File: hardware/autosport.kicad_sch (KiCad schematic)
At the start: 12 parts, among them J2 AS022-55SN

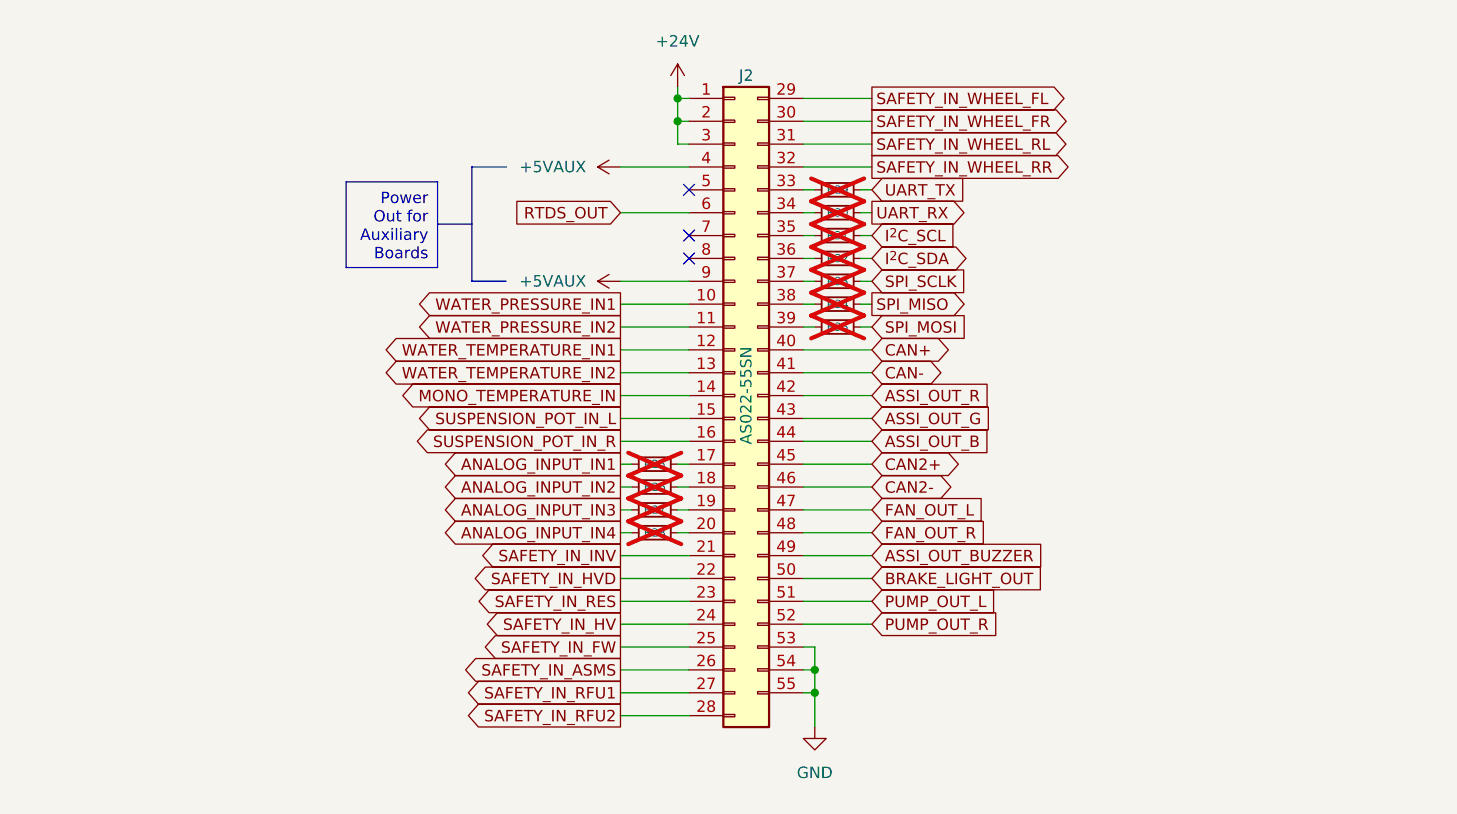
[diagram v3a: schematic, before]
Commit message: Improve the schematic according to the feedback
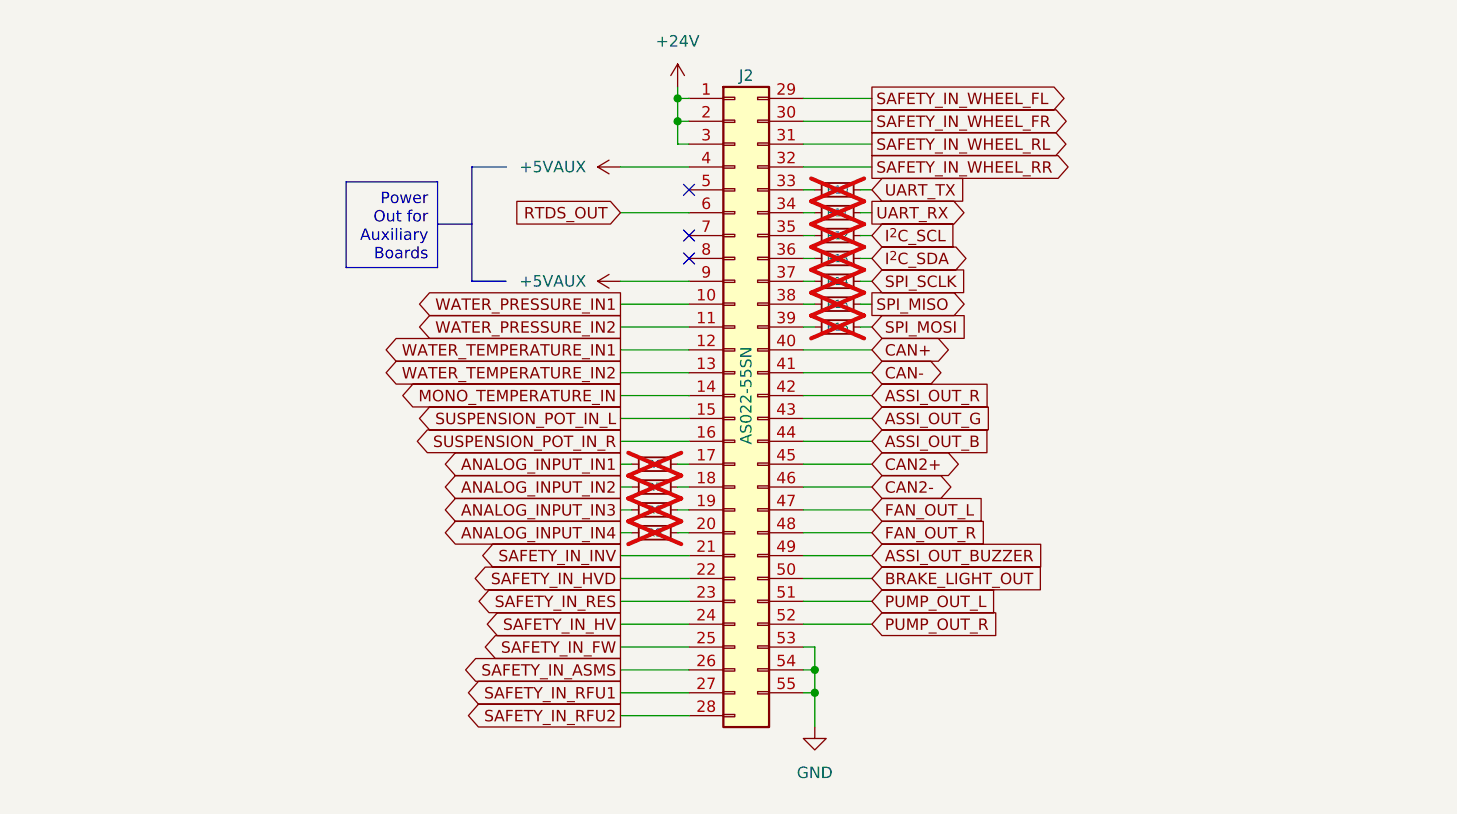
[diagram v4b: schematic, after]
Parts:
- renumbered R29 to R10, R30 to R11, R31 to R12, R32 to R13, R33 to R14, R34 to R15, R35 to R16, R25 to R6, R26 to R7, R27 to R8, R28 to R9
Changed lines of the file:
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@@
   (symbol (lib_id "Device:R_Small") (at 160.02 80.01 90) (unit 1)
     (in_bom yes) (on_board yes) (dnp yes)
-    (property "Reference" "R30" (at 160.02 80.01 90)
+    (property "Reference" "R11" (at 160.02 80.01 90)
       (effects (font (size 0.9 0.9)))
     )
@@
       (project "rearbox"
         (path "/b652b05a-4e3d-4ad1-b032-18886abe7d45/cf65c657-8245-46fb-8929-d241bd579513"
-          (reference "R30") (unit 1)
+          (reference "R11") (unit 1)
         )
       )
@@
   (symbol (lib_id "Device:R_Small") (at 160.02 87.63 90) (unit 1)
     (in_bom yes) (on_board yes) (dnp yes)
-    (property "Reference" "R33" (at 160.02 87.63 90)
+    (property "Reference" "R14" (at 160.02 87.63 90)
       (effects (font (size 0.9 0.9)))
     )
@@
       (project "rearbox"
         (path "/b652b05a-4e3d-4ad1-b032-18886abe7d45/cf65c657-8245-46fb-8929-d241bd579513"
-          (reference "R33") (unit 1)
+          (reference "R14") (unit 1)
         )
       )
@@
   (symbol (lib_id "Power_Ports:+5VAUX") (at 135.89 74.93 90) (unit 1)
     (in_bom yes) (on_board yes) (dnp no) (fields_autoplaced)
-    (property "Reference" "#PWR056" (at 139.7 74.93 0)
+    (property "Reference" "#PWR045" (at 139.7 74.93 0)
       (effects (font (size 1.27 1.27)) hide)
     )
@@
       (project "rearbox"
         (path "/b652b05a-4e3d-4ad1-b032-18886abe7d45/cf65c657-8245-46fb-8929-d241bd579513"
-          (reference "#PWR056") (unit 1)
+          (reference "#PWR045") (unit 1)
         )
       )
@@
   (symbol (lib_id "Device:R_Small") (at 160.02 82.55 90) (unit 1)
     (in_bom yes) (on_board yes) (dnp yes)
-    (property "Reference" "R31" (at 160.02 82.55 90)
+    (property "Reference" "R12" (at 160.02 82.55 90)
       (effects (font (size 0.9 0.9)))
     )
@@
       (project "rearbox"
         (path "/b652b05a-4e3d-4ad1-b032-18886abe7d45/cf65c657-8245-46fb-8929-d241bd579513"
-          (reference "R31") (unit 1)
+          (reference "R12") (unit 1)
         )
       )
@@
   (symbol (lib_id "power:+24V") (at 142.24 66.04 0) (unit 1)
     (in_bom yes) (on_board yes) (dnp no)
-    (property "Reference" "#PWR058" (at 142.24 69.85 0)
+    (property "Reference" "#PWR047" (at 142.24 69.85 0)
       (effects (font (size 1.27 1.27)) hide)
     )
@@
       (project "rearbox"
         (path "/b652b05a-4e3d-4ad1-b032-18886abe7d45/cf65c657-8245-46fb-8929-d241bd579513"
-          (reference "#PWR058") (unit 1)
+          (reference "#PWR047") (unit 1)
         )
       )
@@
   (symbol (lib_id "Device:R_Small") (at 160.02 77.47 90) (unit 1)
     (in_bom yes) (on_board yes) (dnp yes)
-    (property "Reference" "R29" (at 160.02 77.47 90)
+    (property "Reference" "R10" (at 160.02 77.47 90)
       (effects (font (size 0.9 0.9)))
     )
@@
       (project "rearbox"
         (path "/b652b05a-4e3d-4ad1-b032-18886abe7d45/cf65c657-8245-46fb-8929-d241bd579513"
-          (reference "R29") (unit 1)
+          (reference "R10") (unit 1)
         )
       )
@@
   (symbol (lib_id "Device:R_Small") (at 139.7 115.57 90) (unit 1)
     (in_bom yes) (on_board yes) (dnp yes)
-    (property "Reference" "R28" (at 139.7 115.57 90)
+    (property "Reference" "R9" (at 139.7 115.57 90)
       (effects (font (size 0.9 0.9)))
     )
@@
       (project "rearbox"
         (path "/b652b05a-4e3d-4ad1-b032-18886abe7d45/cf65c657-8245-46fb-8929-d241bd579513"
-          (reference "R28") (unit 1)
+          (reference "R9") (unit 1)
         )
       )
@@
   (symbol (lib_id "Power_Ports:+5VAUX") (at 135.89 87.63 90) (unit 1)
     (in_bom yes) (on_board yes) (dnp no) (fields_autoplaced)
-    (property "Reference" "#PWR057" (at 139.7 87.63 0)
+    (property "Reference" "#PWR046" (at 139.7 87.63 0)
       (effects (font (size 1.27 1.27)) hide)
     )
@@
       (project "rearbox"
         (path "/b652b05a-4e3d-4ad1-b032-18886abe7d45/cf65c657-8245-46fb-8929-d241bd579513"
-          (reference "#PWR057") (unit 1)
+          (reference "#PWR046") (unit 1)
         )
       )
@@
   (symbol (lib_id "Device:R_Small") (at 160.02 85.09 90) (unit 1)
     (in_bom yes) (on_board yes) (dnp yes)
-    (property "Reference" "R32" (at 160.02 85.09 90)
+    (property "Reference" "R13" (at 160.02 85.09 90)
       (effects (font (size 0.9 0.9)))
     )
@@
       (project "rearbox"
         (path "/b652b05a-4e3d-4ad1-b032-18886abe7d45/cf65c657-8245-46fb-8929-d241bd579513"
-          (reference "R32") (unit 1)
+          (reference "R13") (unit 1)
         )
       )
@@
   (symbol (lib_id "Device:R_Small") (at 139.7 110.49 90) (unit 1)
     (in_bom yes) (on_board yes) (dnp yes)
-    (property "Reference" "R26" (at 139.7 110.49 90)
+    (property "Reference" "R7" (at 139.7 110.49 90)
       (effects (font (size 0.9 0.9)))
     )
@@
       (project "rearbox"
         (path "/b652b05a-4e3d-4ad1-b032-18886abe7d45/cf65c657-8245-46fb-8929-d241bd579513"
-          (reference "R26") (unit 1)
+          (reference "R7") (unit 1)
         )
       )
@@
   (symbol (lib_id "power:GND") (at 157.48 137.16 0) (unit 1)
     (in_bom yes) (on_board yes) (dnp no) (fields_autoplaced)
-    (property "Reference" "#PWR059" (at 157.48 143.51 0)
+    (property "Reference" "#PWR048" (at 157.48 143.51 0)
       (effects (font (size 1.27 1.27)) hide)
     )
@@
       (project "rearbox"
         (path "/b652b05a-4e3d-4ad1-b032-18886abe7d45/cf65c657-8245-46fb-8929-d241bd579513"
-          (reference "#PWR059") (unit 1)
+          (reference "#PWR048") (unit 1)
         )
       )
@@
   (symbol (lib_id "Device:R_Small") (at 139.7 107.95 90) (unit 1)
     (in_bom yes) (on_board yes) (dnp yes)
-    (property "Reference" "R25" (at 139.7 107.95 90)
+    (property "Reference" "R6" (at 139.7 107.95 90)
       (effects (font (size 0.9 0.9)))
     )
@@
       (project "rearbox"
         (path "/b652b05a-4e3d-4ad1-b032-18886abe7d45/cf65c657-8245-46fb-8929-d241bd579513"
-          (reference "R25") (unit 1)
+          (reference "R6") (unit 1)
         )
       )
@@
   (symbol (lib_id "Device:R_Small") (at 160.02 90.17 90) (unit 1)
     (in_bom yes) (on_board yes) (dnp yes)
-    (property "Reference" "R34" (at 160.02 90.17 90)
+    (property "Reference" "R15" (at 160.02 90.17 90)
       (effects (font (size 0.9 0.9)))
     )
@@
       (project "rearbox"
         (path "/b652b05a-4e3d-4ad1-b032-18886abe7d45/cf65c657-8245-46fb-8929-d241bd579513"
-          (reference "R34") (unit 1)
+          (reference "R15") (unit 1)
         )
       )
@@
   (symbol (lib_id "Device:R_Small") (at 139.7 113.03 90) (unit 1)
     (in_bom yes) (on_board yes) (dnp yes)
-    (property "Reference" "R27" (at 139.7 113.03 90)
+    (property "Reference" "R8" (at 139.7 113.03 90)
       (effects (font (size 0.9 0.9)))
     )
@@
       (project "rearbox"
         (path "/b652b05a-4e3d-4ad1-b032-18886abe7d45/cf65c657-8245-46fb-8929-d241bd579513"
-          (reference "R27") (unit 1)
+          (reference "R8") (unit 1)
         )
       )
@@
   (symbol (lib_id "Device:R_Small") (at 160.02 92.71 90) (unit 1)
     (in_bom yes) (on_board yes) (dnp yes)
-    (property "Reference" "R35" (at 160.02 92.71 90)
+    (property "Reference" "R16" (at 160.02 92.71 90)
       (effects (font (size 0.9 0.9)))
     )
@@
       (project "rearbox"
         (path "/b652b05a-4e3d-4ad1-b032-18886abe7d45/cf65c657-8245-46fb-8929-d241bd579513"
-          (reference "R35") (unit 1)
-        )
-      )
+          (reference "R16") (unit 1)
+        )
+      )

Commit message: Add high-side drivers to the fans and pumps
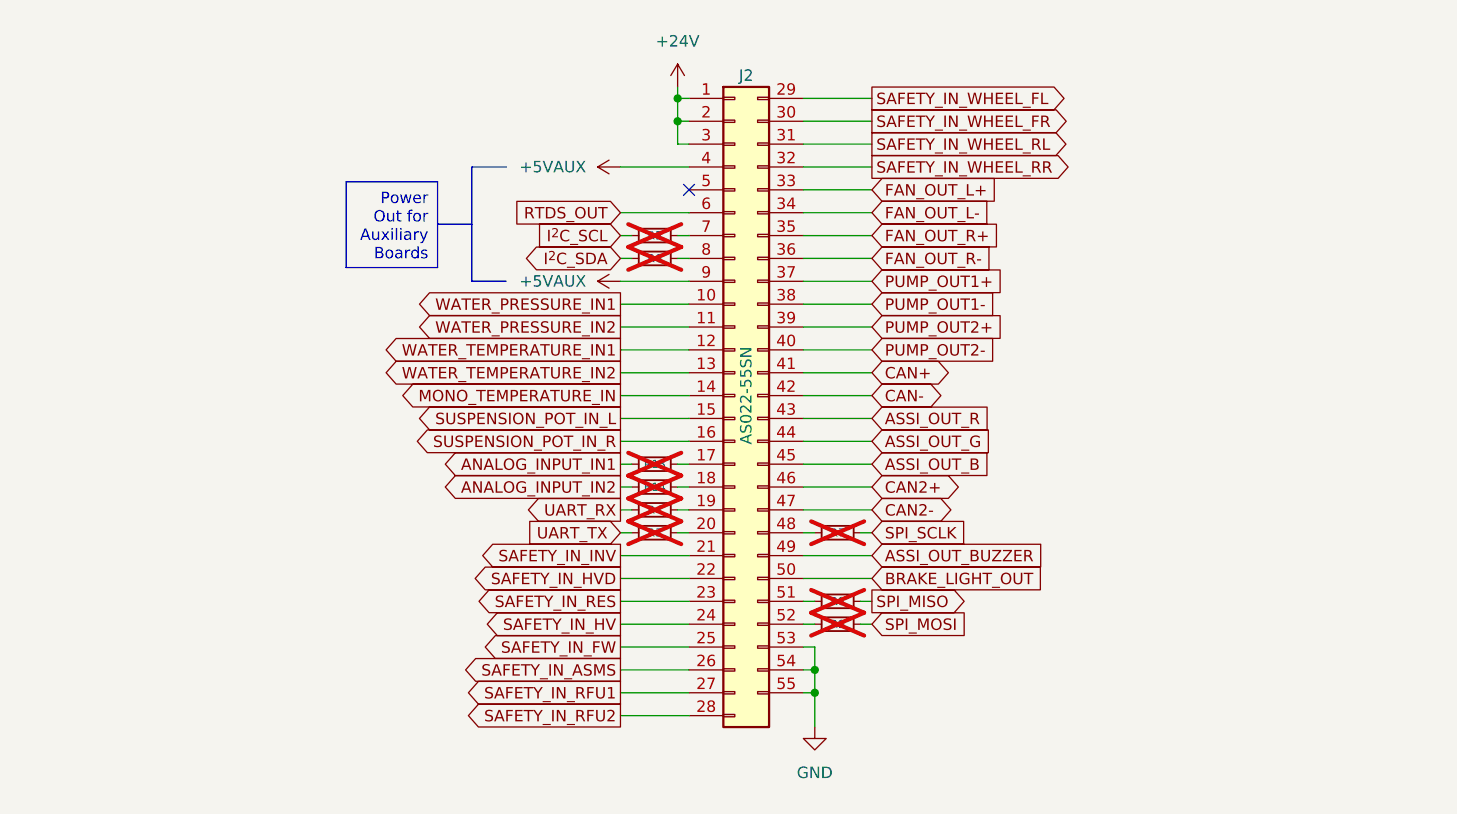
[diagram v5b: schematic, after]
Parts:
- removed R10, R11, R12, R13, R14, R15, R16: 0R, Resistor_SMD:R_0603_1608Metric, symbol Device:R_Small
- added R3, R4, R5, R6, R7: 0R, Resistor_SMD:R_0603_1608Metric, symbol Device:R_Small
- renumbered R6 to R13, R7 to R14
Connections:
- net FAN_OUT_L is gone; now on net CAN2-: J2.47 (Pin_47)
- net PUMP_OUT_L is gone; now on an unnamed net: J2.51 (Pin_51)
- net PUMP_OUT_R is gone; now on an unnamed net: J2.52 (Pin_52)
- net ASSI_OUT_B: now also J2.45 (Pin_45); no longer J2.44 (Pin_44)
- net ASSI_OUT_G: now also J2.44 (Pin_44); no longer J2.43 (Pin_43)
- net ASSI_OUT_R: now also J2.43 (Pin_43); no longer J2.42 (Pin_42)
- net CAN+: now also J2.41 (Pin_41); no longer J2.40 (Pin_40)
- net CAN-: now also J2.42 (Pin_42); no longer J2.41 (Pin_41)
- net CAN2+: now also J2.46 (Pin_46); no longer J2.45 (Pin_45)
- net CAN2-: no longer J2.46 (Pin_46)
- net I^{2}C_SCL: now also R5.2
- net I^{2}C_SDA: now also R6.2
- net SPI_MISO: now also R8.2
- net SPI_MOSI: now also R9.2
- net SPI_SCLK: now also R7.2
- net UART_RX: now also R4.2
- net UART_TX: now also R3.2
- net FAN_OUT_L-: now reaches J2.34 (Pin_34)
- net at J2.19 (Pin_19): now also R4.1; no longer R8.2
- net at J2.20 (Pin_20): now also R3.1; no longer R9.2
- net FAN_OUT_L+: now reaches J2.33 (Pin_33)
- net FAN_OUT_R+: now reaches J2.35 (Pin_35)
- net FAN_OUT_R-: now reaches J2.36 (Pin_36)
- net PUMP_OUT1+: now reaches J2.37 (Pin_37)
- net PUMP_OUT1-: now reaches J2.38 (Pin_38)
- net PUMP_OUT2+: now reaches J2.39 (Pin_39)
- net at J2.7 (Pin_7): now also R5.1
- net at J2.8 (Pin_8): now also R6.1
- net ANALOG_INPUT_IN3: no longer names the net of R8.1
- net ANALOG_INPUT_IN4: no longer names the net of R9.1
- net FAN_OUT_R: no longer names the net of J2.48 (Pin_48)
- net FAN_OUT_R: now also R7.1
- new net PUMP_OUT2-: J2.40 (Pin_40)
- no-connect marks 3 -> 1

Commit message: Use in-amps
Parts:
- renumbered R4 to R10, R3 to R11, R7 to R12, R8 to R13, R9 to R14, R5 to R6, R6 to R7, R13 to R8, R14 to R9
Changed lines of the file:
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@@
   (symbol (lib_id "Device:R_Small") (at 139.7 85.09 270) (mirror x) (unit 1)
     (in_bom yes) (on_board yes) (dnp yes)
-    (property "Reference" "R6" (at 139.7 85.09 90)
+    (property "Reference" "R7" (at 139.7 85.09 90)
       (effects (font (size 0.9 0.9)))
     )
@@
       (project "rearbox"
         (path "/b652b05a-4e3d-4ad1-b032-18886abe7d45/cf65c657-8245-46fb-8929-d241bd579513"
+          (reference "R7") (unit 1)
+        )
+        (path "/b652b05a-4e3d-4ad1-b032-18886abe7d45"
           (reference "R6") (unit 1)
         )
-        (path "/b652b05a-4e3d-4ad1-b032-18886abe7d45"
-          (reference "R6") (unit 1)
-        )
       )
     )
@@
   (symbol (lib_id "Device:R_Small") (at 160.02 123.19 90) (unit 1)
     (in_bom yes) (on_board yes) (dnp yes)
-    (property "Reference" "R8" (at 160.02 123.19 90)
+    (property "Reference" "R13" (at 160.02 123.19 90)
       (effects (font (size 0.9 0.9)))
     )
@@
       (project "rearbox"
         (path "/b652b05a-4e3d-4ad1-b032-18886abe7d45/cf65c657-8245-46fb-8929-d241bd579513"
-          (reference "R8") (unit 1)
+          (reference "R13") (unit 1)
         )
         (path "/b652b05a-4e3d-4ad1-b032-18886abe7d45"
@@
   (symbol (lib_id "Device:R_Small") (at 139.7 82.55 270) (mirror x) (unit 1)
     (in_bom yes) (on_board yes) (dnp yes)
-    (property "Reference" "R5" (at 139.7 82.55 90)
+    (property "Reference" "R6" (at 139.7 82.55 90)
       (effects (font (size 0.9 0.9)))
     )
@@
       (project "rearbox"
         (path "/b652b05a-4e3d-4ad1-b032-18886abe7d45/cf65c657-8245-46fb-8929-d241bd579513"
+          (reference "R6") (unit 1)
+        )
+        (path "/b652b05a-4e3d-4ad1-b032-18886abe7d45"
           (reference "R5") (unit 1)
         )
-        (path "/b652b05a-4e3d-4ad1-b032-18886abe7d45"
-          (reference "R5") (unit 1)
-        )
       )
     )
@@
   (symbol (lib_id "Device:R_Small") (at 160.02 115.57 90) (unit 1)
     (in_bom yes) (on_board yes) (dnp yes)
-    (property "Reference" "R7" (at 160.02 115.57 90)
+    (property "Reference" "R12" (at 160.02 115.57 90)
       (effects (font (size 0.9 0.9)))
     )
@@
       (project "rearbox"
         (path "/b652b05a-4e3d-4ad1-b032-18886abe7d45/cf65c657-8245-46fb-8929-d241bd579513"
-          (reference "R7") (unit 1)
+          (reference "R12") (unit 1)
         )
         (path "/b652b05a-4e3d-4ad1-b032-18886abe7d45"
@@
   (symbol (lib_id "Device:R_Small") (at 139.7 110.49 90) (unit 1)
     (in_bom yes) (on_board yes) (dnp yes)
-    (property "Reference" "R14" (at 139.7 110.49 90)
+    (property "Reference" "R9" (at 139.7 110.49 90)
       (effects (font (size 0.9 0.9)))
     )
@@
       (project "rearbox"
         (path "/b652b05a-4e3d-4ad1-b032-18886abe7d45/cf65c657-8245-46fb-8929-d241bd579513"
-          (reference "R14") (unit 1)
+          (reference "R9") (unit 1)
         )
       )
@@
   (symbol (lib_id "Device:R_Small") (at 139.7 115.57 270) (unit 1)
     (in_bom yes) (on_board yes) (dnp yes)
-    (property "Reference" "R3" (at 139.7 115.57 90)
+    (property "Reference" "R11" (at 139.7 115.57 90)
       (effects (font (size 0.9 0.9)))
     )
@@
       (project "rearbox"
         (path "/b652b05a-4e3d-4ad1-b032-18886abe7d45/cf65c657-8245-46fb-8929-d241bd579513"
-          (reference "R3") (unit 1)
+          (reference "R11") (unit 1)
         )
         (path "/b652b05a-4e3d-4ad1-b032-18886abe7d45"
@@
   (symbol (lib_id "Device:R_Small") (at 139.7 107.95 90) (unit 1)
     (in_bom yes) (on_board yes) (dnp yes)
-    (property "Reference" "R13" (at 139.7 107.95 90)
+    (property "Reference" "R8" (at 139.7 107.95 90)
       (effects (font (size 0.9 0.9)))
     )
@@
       (project "rearbox"
         (path "/b652b05a-4e3d-4ad1-b032-18886abe7d45/cf65c657-8245-46fb-8929-d241bd579513"
-          (reference "R13") (unit 1)
+          (reference "R8") (unit 1)
         )
       )
@@
   (symbol (lib_id "Device:R_Small") (at 160.02 125.73 90) (unit 1)
     (in_bom yes) (on_board yes) (dnp yes)
-    (property "Reference" "R9" (at 160.02 125.73 90)
+    (property "Reference" "R14" (at 160.02 125.73 90)
       (effects (font (size 0.9 0.9)))
     )
@@
       (project "rearbox"
         (path "/b652b05a-4e3d-4ad1-b032-18886abe7d45/cf65c657-8245-46fb-8929-d241bd579513"
+          (reference "R14") (unit 1)
+        )
+        (path "/b652b05a-4e3d-4ad1-b032-18886abe7d45"
           (reference "R9") (unit 1)
         )
-        (path "/b652b05a-4e3d-4ad1-b032-18886abe7d45"
-          (reference "R9") (unit 1)
-        )
       )
     )
@@
   (symbol (lib_id "Device:R_Small") (at 139.7 113.03 270) (unit 1)
     (in_bom yes) (on_board yes) (dnp yes)
-    (property "Reference" "R4" (at 139.7 113.03 90)
+    (property "Reference" "R10" (at 139.7 113.03 90)
       (effects (font (size 0.9 0.9)))
     )
@@
       (project "rearbox"
         (path "/b652b05a-4e3d-4ad1-b032-18886abe7d45/cf65c657-8245-46fb-8929-d241bd579513"
-          (reference "R4") (unit 1)
-        )
-        (path "/b652b05a-4e3d-4ad1-b032-18886abe7d45"
+          (reference "R10") (unit 1)
+        )
+        (path "/b652b05a-4e3d-4ad1-b032-18886abe7d45"
